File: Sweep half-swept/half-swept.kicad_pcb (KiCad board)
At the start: 2 copper layers, 109 x 86.9 mm, 25 parts, among them J2 AudioJack4dpb, SW1 SW_Push, SW10 SW_Push, SW11 SW_Push, SW12 SW_Push, SW13 SW_Push, SW14 SW_Push, SW15 SW_Push, SW16 SW_Push, SW17 SW_Push, SW2 SW_Push, SW3 SW_Push, SW4 SW_Push, SW5 SW_Push, SW6 SW_Push, SW7 SW_Push, SW8 SW_Push, SW9 SW_Push, U1 ProMicro-kbd

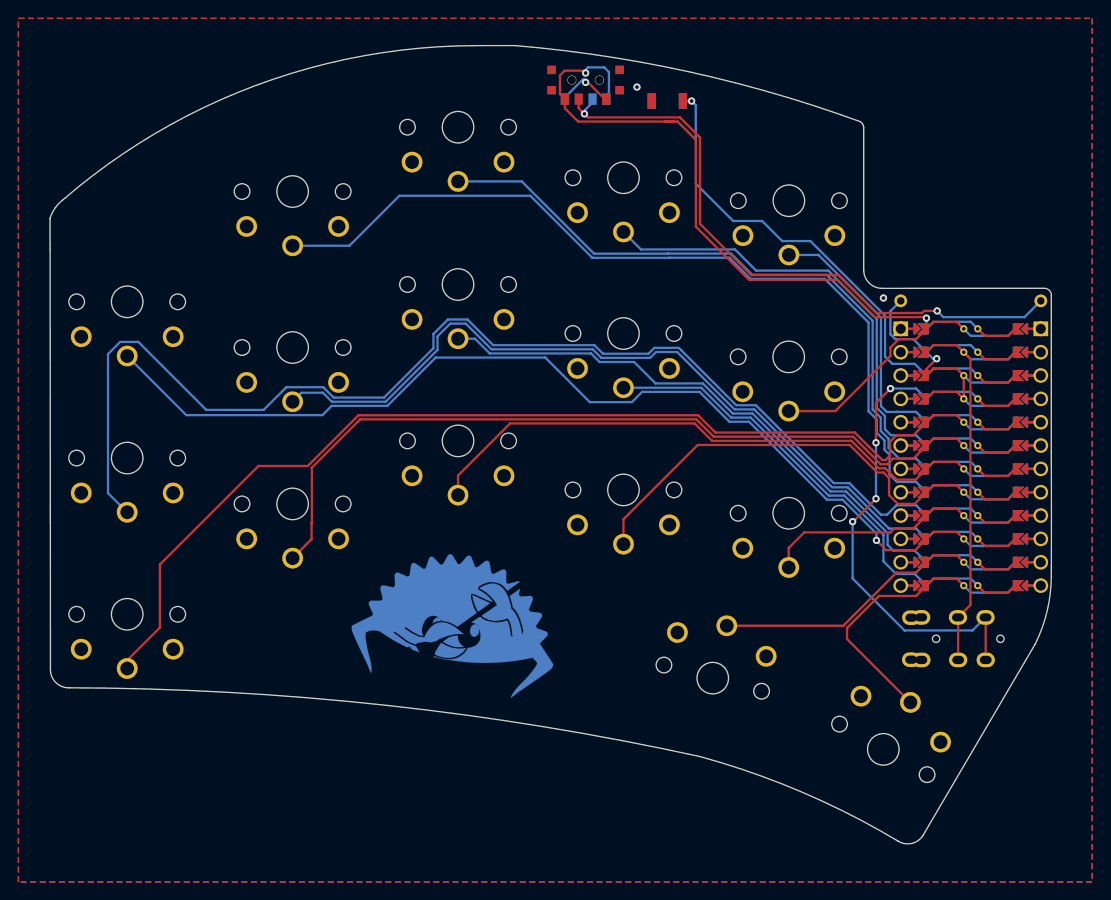
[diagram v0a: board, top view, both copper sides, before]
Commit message: Pull in the edge cut
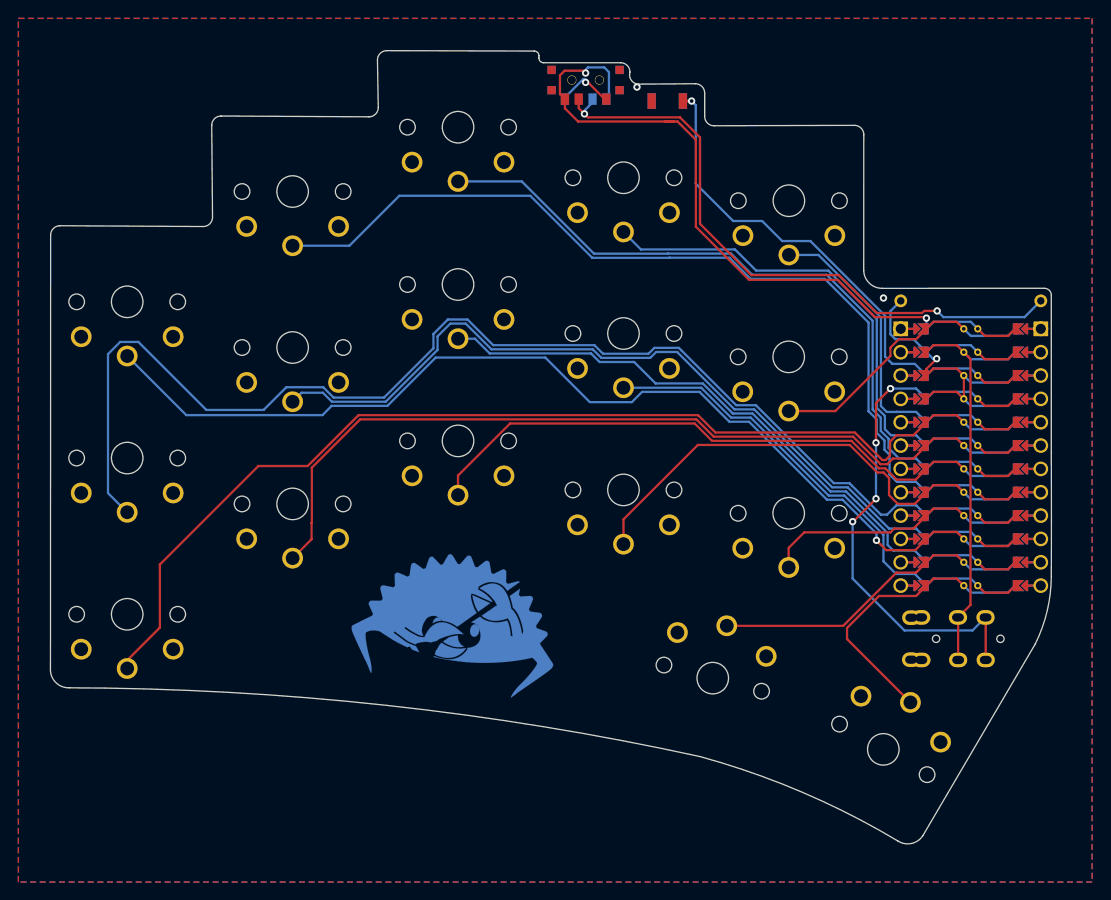
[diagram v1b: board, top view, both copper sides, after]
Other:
- board size 109 x 86.9 mm -> 108.9 x 86.3 mm
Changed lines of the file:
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@@
   )
   (gr_arc (start 126.885 44.612) (mid 127.41533 44.83167) (end 127.635 45.362) (layer "Edge.Cuts") (width 0.05))
-  (gr_line (start 18.690055 36.976702) (end 18.730254 86.245024) (layer "Edge.Cuts") (width 0.05))
-  (gr_arc (start 106.78729 26.456889) (mid 107.104079 26.733645) (end 107.222045 27.137419) (layer "Edge.Cuts") (width 0.05))
+  (gr_line (start 18.75242 38.81842) (end 18.730254 86.245024) (layer "Edge.Cuts") (width 0.05))
   (gr_arc (start 89.409134 95.561946) (mid 100.486488 99.421597) (end 110.938 104.748) (layer "Edge.Cuts") (width 0.05))
-  (gr_arc (start 18.690055 36.976702) (mid 19.246929 35.858882) (end 20.117 34.963) (layer "Edge.Cuts") (width 0.05))
   (gr_arc (start 109.257002 44.614917) (mid 107.844534 44.065716) (end 107.222001 42.683999) (layer "Edge.Cuts") (width 0.05))
-  (gr_arc (start 69.291777 18.200679) (mid 88.315879 21.073764) (end 106.78729 26.456889) (layer "Edge.Cuts") (width 0.05))
   (gr_arc (start 113.67 104.149265) (mid 112.428995 105.01898) (end 110.938 104.748) (layer "Edge.Cuts") (width 0.05))
   (gr_arc (start 20.768 88.081119) (mid 55.288442 89.987554) (end 89.409134 95.561946) (layer "Edge.Cuts") (width 0.05))
   (gr_arc (start 20.768 88.081119) (mid 19.380573 87.572102) (end 18.730254 86.245024) (layer "Edge.Cuts") (width 0.05))
   (gr_line (start 127.635 45.362) (end 127.635 62.484) (layer "Edge.Cuts") (width 0.05))
-  (gr_line (start 107.222001 42.683999) (end 107.222045 27.137419) (layer "Edge.Cuts") (width 0.05))
+  (gr_line (start 107.222001 42.683999) (end 107.23158 27.89642) (layer "Edge.Cuts") (width 0.05))
   (gr_line (start 109.257002 44.614917) (end 126.885 44.612) (layer "Edge.Cuts") (width 0.05))
-  (gr_arc (start 20.117 34.963) (mid 41.093524 22.531455) (end 65.090389 18.206139) (layer "Edge.Cuts") (width 0.05))
   (gr_line (start 125.888304 83.312) (end 113.67 104.149265) (layer "Edge.Cuts") (width 0.05))
   (gr_arc (start 127.635 75.98785) (mid 127.177913 79.749197) (end 125.888304 83.312) (layer "Edge.Cuts") (width 0.05))
-  (gr_line (start 69.291777 18.200679) (end 65.090389 18.206139) (layer "Edge.Cuts") (width 0.05))
   (gr_line (start 127.635 62.484) (end 127.647 69.85) (layer "Edge.Cuts") (width 0.05))
   (gr_line (start 127.647 69.85) (end 127.635 75.98785) (layer "Edge.Cuts") (width 0.05))
+  (gr_line (start 71.882 19.558) (end 71.882 19.304) (layer "Edge.Cuts") (width 0.05))
+  (gr_arc (start 90.932 26.924) (mid 90.21358 26.62642) (end 89.916 25.908) (layer "Edge.Cuts") (width 0.05))
+  (gr_line (start 37.29442 25.86442) (end 53.38358 25.95158) (layer "Edge.Cuts") (width 0.05))
+  (gr_arc (start 54.39958 24.93558) (mid 54.102 25.654) (end 53.38358 25.95158) (layer "Edge.Cuts") (width 0.05))
+  (gr_arc (start 88.9 22.352) (mid 89.61842 22.64958) (end 89.916 23.368) (layer "Edge.Cuts") (width 0.05))
+  (gr_arc (start 54.31242 19.76842) (mid 54.61 19.05) (end 55.32842 18.75242) (layer "Edge.Cuts") (width 0.05))
+  (gr_arc (start 71.374 18.796) (mid 71.73321 18.94479) (end 71.882 19.304) (layer "Edge.Cuts") (width 0.05))
+  (gr_arc (start 82.76042 22.39558) (mid 82.042 22.098) (end 81.74442 21.37958) (layer "Edge.Cuts") (width 0.05))
+  (gr_line (start 106.21558 26.88042) (end 90.932 26.924) (layer "Edge.Cuts") (width 0.05))
+  (gr_line (start 36.27842 26.88042) (end 36.36558 36.87358) (layer "Edge.Cuts") (width 0.05))
+  (gr_arc (start 18.75242 38.81842) (mid 19.05 38.1) (end 19.76842 37.80242) (layer "Edge.Cuts") (width 0.05))
+  (gr_line (start 19.76842 37.80242) (end 35.34958 37.88958) (layer "Edge.Cuts") (width 0.05))
+  (gr_arc (start 106.21558 26.88042) (mid 106.934 27.178) (end 107.23158 27.89642) (layer "Edge.Cuts") (width 0.05))
+  (gr_arc (start 80.772 20.066) (mid 81.49042 20.36358) (end 81.788 21.082) (layer "Edge.Cuts") (width 0.05))
+  (gr_line (start 55.32842 18.75242) (end 71.374 18.796) (layer "Edge.Cuts") (width 0.05))
+  (gr_line (start 89.916 25.908) (end 89.916 23.368) (layer "Edge.Cuts") (width 0.05))
+  (gr_line (start 54.39958 24.93558) (end 54.31242 19.76842) (layer "Edge.Cuts") (width 0.05))
+  (gr_line (start 88.9 22.352) (end 82.76042 22.39558) (layer "Edge.Cuts") (width 0.05))
+  (gr_arc (start 36.27842 26.88042) (mid 36.576 26.162) (end 37.29442 25.86442) (layer "Edge.Cuts") (width 0.05))
+  (gr_arc (start 36.36558 36.87358) (mid 36.068 37.592) (end 35.34958 37.88958) (layer "Edge.Cuts") (width 0.05))
+  (gr_arc (start 72.39 20.066) (mid 72.03079 19.91721) (end 71.882 19.558) (layer "Edge.Cuts") (width 0.05))
+  (gr_line (start 81.788 21.082) (end 81.74442 21.37958) (layer "Edge.Cuts") (width 0.05))
+  (gr_line (start 80.772 20.066) (end 72.39 20.066) (layer "Edge.Cuts") (width 0.05))
   (segment (start 114.046 53.3908) (end 115.1636 52.2732) (width 0.25) (layer "F.Cu") (net 1))
   (segment (start 118.11 56.642) (end 118.11 54.102) (width 0.25) (layer "F.Cu") (net 1))
